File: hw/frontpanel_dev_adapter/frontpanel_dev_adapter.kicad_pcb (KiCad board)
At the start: 4 copper layers, 100 x 100 mm, 130 parts, among them J201 KLD-0202-A, J202 Conn_WR-FAST_01x04, J203 Molex_MicroFit_30-43045-0421, J301 FFC_conn_14p, J302 FFC_conn_14p, J303 JST_S2B-PH-SM4-TB, J501 Conn_01x20, J502 Conn_01x20, J503 SWD, J504 STX-3501-3N_(TTL-232R-xV-AJ), J601 Conn_02x32_Odd_Even, J602 Conn_02x32_Odd_Even, J603 Conn_02x32_Odd_Even, J604 Conn_02x32_Odd_Even, M401 Fan_4pin, Q201 Si4497DY, Q301 DMG1012T, Q401 DMG1012T, Q501 AO3401A, SW501 SKHUxxE010, U201 TPS54332DDA, U202 TLV1117LV30DCY, U203 TLV1117LV30DCY, U301 TLV9051SIDBV, U401 74LVC2G17gw, U501 STM32F103CBTx, U502 W25Q64FV, U503 CAT24C256, U504 DS3231MZ, Y501 8.0M

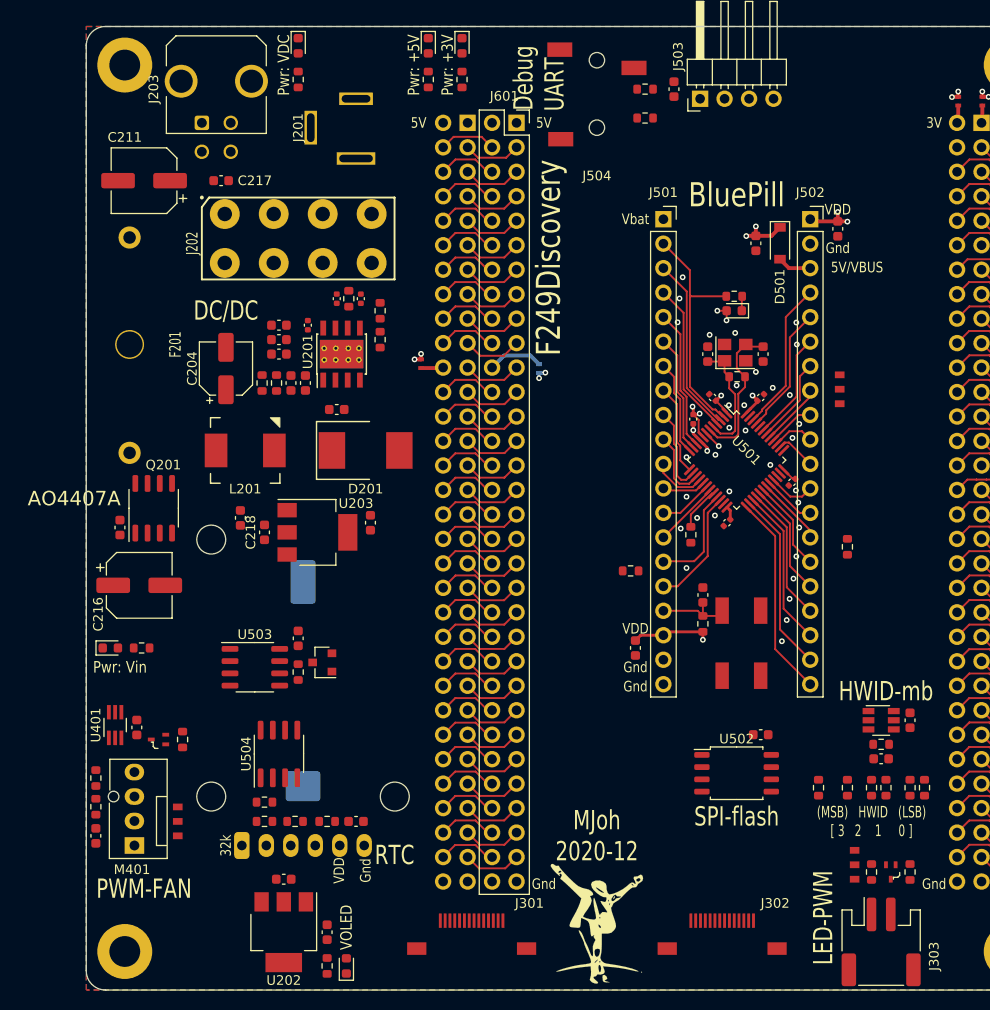
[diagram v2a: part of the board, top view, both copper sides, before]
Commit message: Frontpanel dev adapter: Optimize some LCSC components for JLC assembly; add some datasheets. Optimize F103 16MHz xtal routing
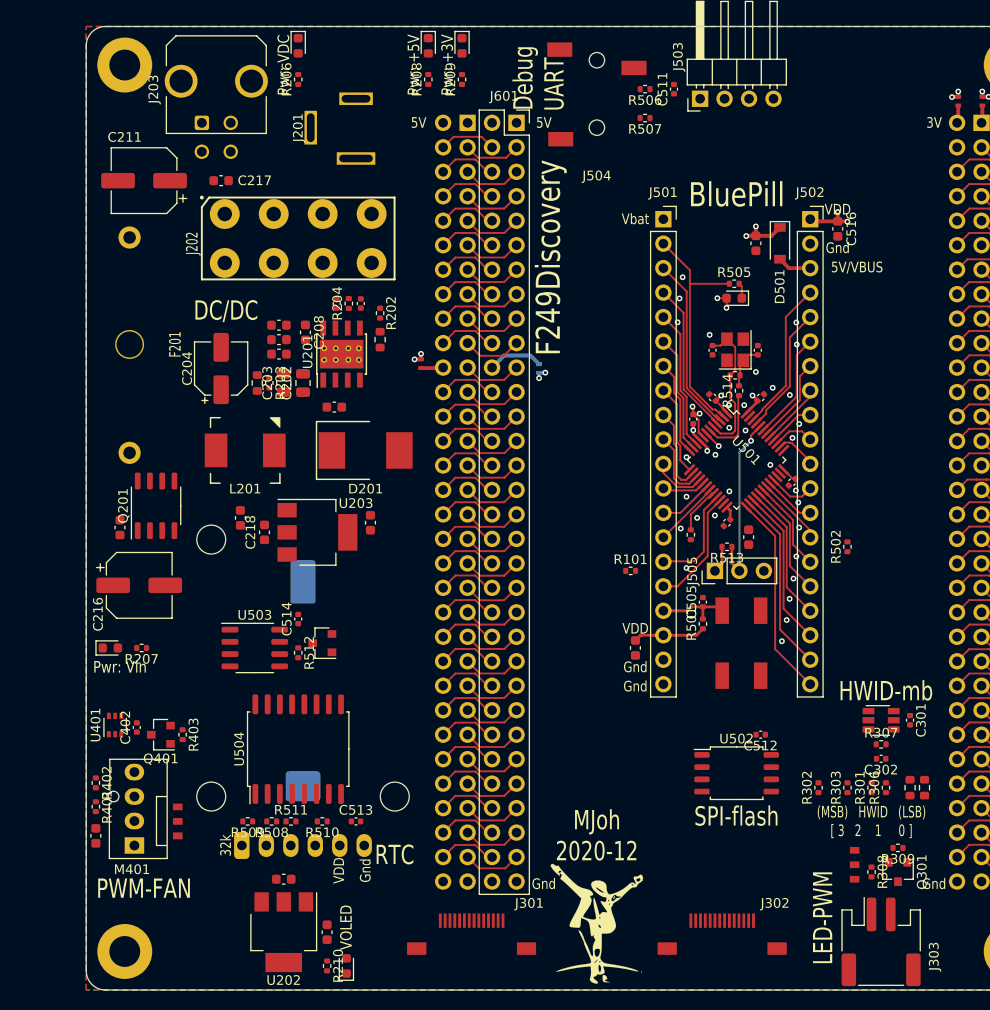
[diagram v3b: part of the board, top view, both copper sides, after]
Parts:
- removed JP501: dogbone_3_ud, customlib_mj_fp:db3_ud_0603
- added C516: 10u, Capacitor_SMD:C_0603_1608Metric, F.Cu at (128.0, 71.0)
- added J505: Conn_01x03, Connector_PinHeader_2.54mm:PinHeader_1x03_P2.54mm_Vertical, F.Cu at (115.2, 106.5)
- added R513: 0R, Resistor_SMD:R_0402_1005Metric, F.Cu at (116.5, 104.0)
- added R514: 47R, Resistor_SMD:R_0402_1005Metric, F.Cu at (117.8, 87.8)
- C202, C203: value 10u -> 10u/16V; footprint Capacitor_SMD:C_0603_1608Metric -> Capacitor_SMD:C_0805_2012Metric
- C205, C206, C207, C212, C218: value 10u -> 10u/10V
- C208: footprint Capacitor_SMD:C_0402_1005Metric -> Capacitor_SMD:C_0603_1608Metric
- C210: value 3n9 -> 3n3
- C301, C302, C402: footprint Capacitor_SMD:C_0603_1608Metric -> Capacitor_SMD:C_0402_1005Metric
- C501, C502, C503, C504, C515: value 0.1u -> 100n
- C505, C511, C512, C513, C514: value 0.1u -> 100n; footprint Capacitor_SMD:C_0603_1608Metric -> Capacitor_SMD:C_0402_1005Metric
- C506, C508: value 20p -> 12p; footprint Capacitor_SMD:C_0603_1608Metric -> Capacitor_SMD:C_0402_1005Metric
- D502: value Green -> White
- Q201: value Si4497DY -> AO4407A
- Q301, Q401: value DMG1012T -> AO3400A; footprint customlib_mj_fp:SOT-523_handsoldering -> Package_TO_SOT_SMD:SOT-23
- R101, R502: value 100 -> 100R; footprint Resistor_SMD:R_0603_1608Metric -> Resistor_SMD:R_0402_1005Metric
- R202, R203, R204, R301, R302, R303, R306, R307, R308, R309, R401, R402, R403, R501, R503, R504, R506, R507, R508, R509, R510, R511, R512: footprint Resistor_SMD:R_0603_1608Metric -> Resistor_SMD:R_0402_1005Metric
- R206, R207: value 4k7 -> 10k; footprint Resistor_SMD:R_0603_1608Metric -> Resistor_SMD:R_0402_1005Metric
- R208: value 1k -> 2k2; footprint Resistor_SMD:R_0603_1608Metric -> Resistor_SMD:R_0402_1005Metric
- R209, R210: value 100R -> 1k; footprint Resistor_SMD:R_0603_1608Metric -> Resistor_SMD:R_0402_1005Metric
- R505: value 1k -> 100R; footprint Resistor_SMD:R_0603_1608Metric -> Resistor_SMD:R_0402_1005Metric
- U401: footprint Package_TO_SOT_SMD:SOT-363_SC-70-6_Handsoldering -> Package_TO_SOT_SMD:SOT-363_SC-70-6
- U502: value W25Q64FV -> W25Q128JVSIQ
- U503: value CAT24C256 -> AT24C256C-SSHL
- U504: value DS3231MZ -> DS3231M; footprint Package_SO:SOIC-8_3.9x4.9mm_P1.27mm -> Package_SO:SOIC-16W_7.5x10.3mm_P1.27mm
- Y501: value 8.0M -> 16MHz
- moved C507 33.3 mm to (118.8, 103.0)
- moved R309 2.80 mm to (134.2, 135.2), turned to 180 degrees
- moved R509 2.65 mm to (66.8, 132.5)
- moved U504 2.06 mm to (72.0, 125.0)
- moved C514 2.00 mm to (72.0, 111.5)
- moved Q501 2.00 mm to (74.5, 114.0)
- moved R512 2.00 mm to (72.0, 115.0)
- moved U503 2.00 mm to (67.5, 114.5)
- moved D502 1.30 mm to (117.2, 78.2)
- moved R505 1.30 mm to (117.2, 76.7)
- moved C208 0.79 mm to (72.8, 81.8)
- moved C203 0.75 mm to (70.5, 87.0)
- moved C505 0.75 mm to (114.0, 109.8)
- moved Q301 0.75 mm to (134.2, 137.8), turned to 270 degrees
- moved R203 0.75 mm to (69.0, 87.0)
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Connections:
- U501 pad 44: GND -> Net-(J505-Pad2)
- U501 pad 6: Net-(C508-Pad1) -> Net-(R514-Pad1)
- U504 pad 2: VDD -> +BATT
- U504 pad 6: +BATT -> GND
- U504 pad 7: I2C1_SDA -> GND
- U504 pad 8: I2C1_SCL -> GND
- Y501 pad 1: Net-(C506-Pad1) -> Net-(C508-Pad1)
- Y501 pad 3: Net-(C508-Pad1) -> Net-(C506-Pad1)
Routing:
- net Net-(J505-Pad2): track 0.00 -> 18.7 mm, vias 0 -> 1
- net Net-(C508-Pad1): track 15.6 -> 4.56 mm
- net Net-(R514-Pad1): track 0.00 -> 7.44 mm
- net GND: track 4.29 -> 7.10 mm, vias 36 -> 34
- net Net-(C506-Pad1): track 12.2 -> 14.7 mm
- net VDD: track 34.5 -> 33.8 mm, vias 21 -> 20
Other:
- board text removed: "AO4407A"

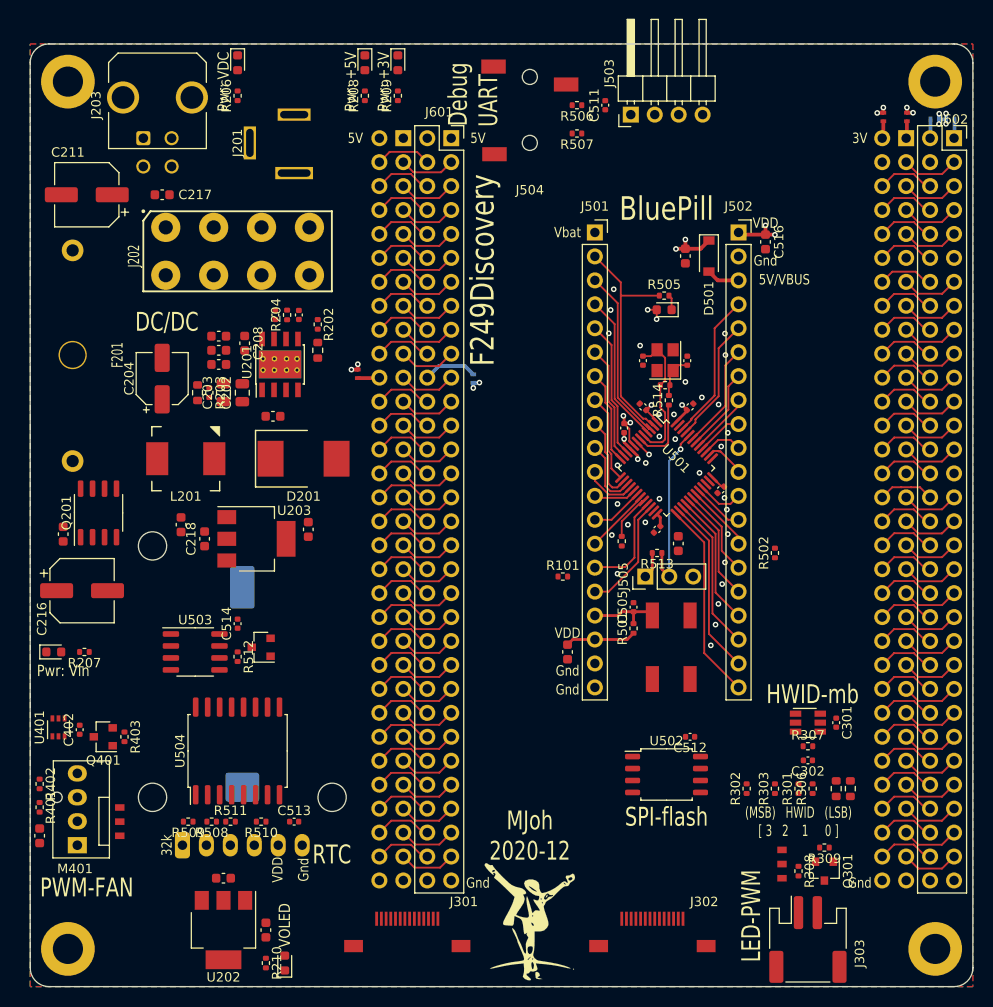
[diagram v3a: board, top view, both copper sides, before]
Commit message: FP adapter/dev board: *routing DONE* ; minor pinout tweaks (optimize routing); fix some missing 3d models
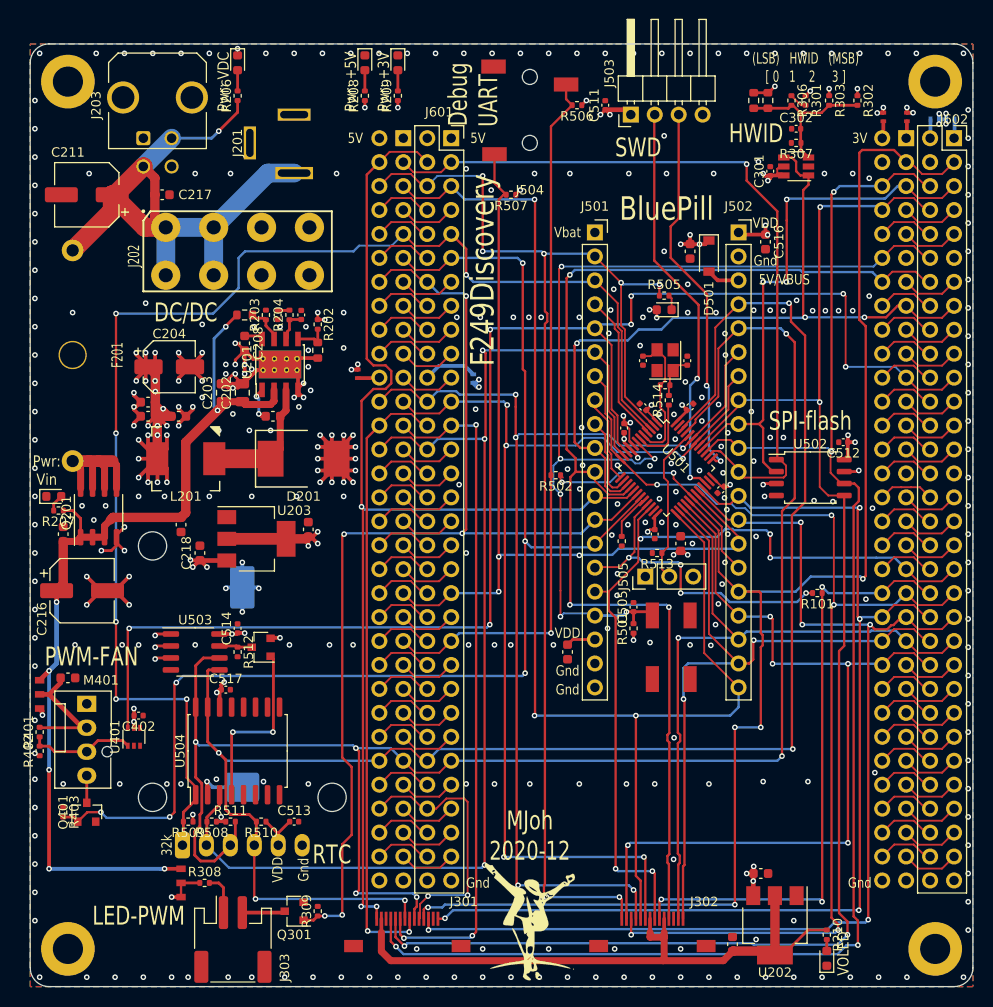
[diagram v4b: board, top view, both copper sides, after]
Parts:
- added C517: 100n, Capacitor_SMD:C_0402_1005Metric, F.Cu at (70.8, 118.5)
- moved R302 73.9 mm to (137.8, 56.0), turned to 270 degrees
- moved R305 73.7 mm to (126.8, 56.0), turned to 270 degrees
- moved R304 73.4 mm to (128.2, 56.0), turned to 270 degrees
- moved R303 73.2 mm to (134.8, 56.0), turned to 270 degrees
- moved R306 73.0 mm to (130.8, 56.0), turned to 270 degrees
- moved R301 73.0 mm to (132.2, 56.0), turned to 270 degrees
- moved C302 67.0 mm to (131.2, 59.0), turned to 0 degrees
- moved R307 64.0 mm to (131.2, 60.5), turned to 180 degrees
- moved JP301 63.8 mm to (66.0, 139.0), turned to 90 degrees
- moved R308 63.0 mm to (68.5, 139.0), turned to 0 degrees
- moved J303 61.0 mm to (71.5, 145.0)
- moved R210 59.6 mm to (134.5, 144.5)
- moved U301 59.0 mm to (131.2, 63.0), turned to 180 degrees
- moved C301 58.9 mm to (128.5, 63.5), turned to 90 degrees
- moved U202 58.5 mm to (129.0, 143.5)
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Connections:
- C401 pad 2: VMAIN -> Net-(C401-Pad2)
- J501 pad 10: HWID_FP -> HWID_MB
- J501 pad 11: HWID_MB -> HWID_FP
- J501 pad 8: ~FP_BTN_1An~ -> /MCU / Bluepill/PA3
- J501 pad 9: ~FP_BTN_1Bn~ -> /MCU / Bluepill/PA4
- J502 pad 12: /MCU / Bluepill/PA12 -> ~FP_BTN_1An~
- J502 pad 13: /MCU / Bluepill/PA11 -> ~FP_BTN_1Bn~
- J601 pad 58: /F429Discovery connection/PG8 -> ~FP_ENC2_SWn~
- J602 pad 54: ~FP_ENC2_SWn~ -> /F429Discovery connection/PD8
- J603 pad 58: /F429Discovery connection/PG8 -> ~FP_ENC2_SWn~
- J604 pad 54: ~FP_ENC2_SWn~ -> /F429Discovery connection/PD8
- JP401 pad 2: VMAIN -> Net-(C401-Pad2)
- M401 pad 2: VMAIN -> Net-(C401-Pad2)
- R401 pad 2: VMAIN -> Net-(C401-Pad2)
- SW501 pad 1: ~RSTn~ -> Net-(SW501-Pad1)
- U501 pad 13: ~FP_BTN_1An~ -> /MCU / Bluepill/PA3
- U501 pad 14: ~FP_BTN_1Bn~ -> /MCU / Bluepill/PA4
- U501 pad 15: HWID_FP -> HWID_MB
- U501 pad 16: HWID_MB -> HWID_FP
- U501 pad 32: /MCU / Bluepill/PA11 -> ~FP_BTN_1Bn~
- U501 pad 33: /MCU / Bluepill/PA12 -> ~FP_BTN_1An~
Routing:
- net I2C1_SCL: track 19.4 -> 184.3 mm, vias 0 -> 6
- net I2C1_SDA: track 21.8 -> 179.3 mm, vias 0 -> 5
- net DISP_FLASH_SCK: track 10.5 -> 161.3 mm, vias 0 -> 4
- net DISP_FLASH_MOSI: track 12.7 -> 159.0 mm, vias 0 -> 4
- net ~DISP_CSn~: track 17.9 -> 155.7 mm, vias 0 -> 5
- net FAN1_RPM: track 20.7 -> 156.6 mm, vias 0 -> 7
- net FAN1_PWM: track 13.0 -> 136.4 mm, vias 0 -> 6
- net 32k: track 24.4 -> 144.1 mm, vias 0 -> 6
- net HWID_FP: track 13.4 -> 127.3 mm, vias 0 -> 3
- net DISP_D~Cn~: track 10.5 -> 122.5 mm, vias 0 -> 3
- net ~SYS_RSTn~: track 27.3 -> 137.3 mm, vias 0 -> 3
- net ~RTC_INTn~_SQW: track 18.3 -> 128.2 mm, vias 0 -> 3
- net AUX_BOOT0: track 31.0 -> 137.3 mm, vias 0 -> 7
- net ~FP_BTN_1Bn~: track 15.1 -> 120.7 mm, vias 0 -> 5
- net PWRBTN_LED_PWM: track 11.7 -> 114.7 mm, vias 0 -> 5
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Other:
- board text added: "(LSB) HWID (MSB) [ 0 1 2 3 ]"
- board text added: "HWID"
- board text added: "SWD"
- board text removed: "(MSB) HWID (LSB) [ 3 2 1 0 ]"
- board text removed: "HWID-mb"

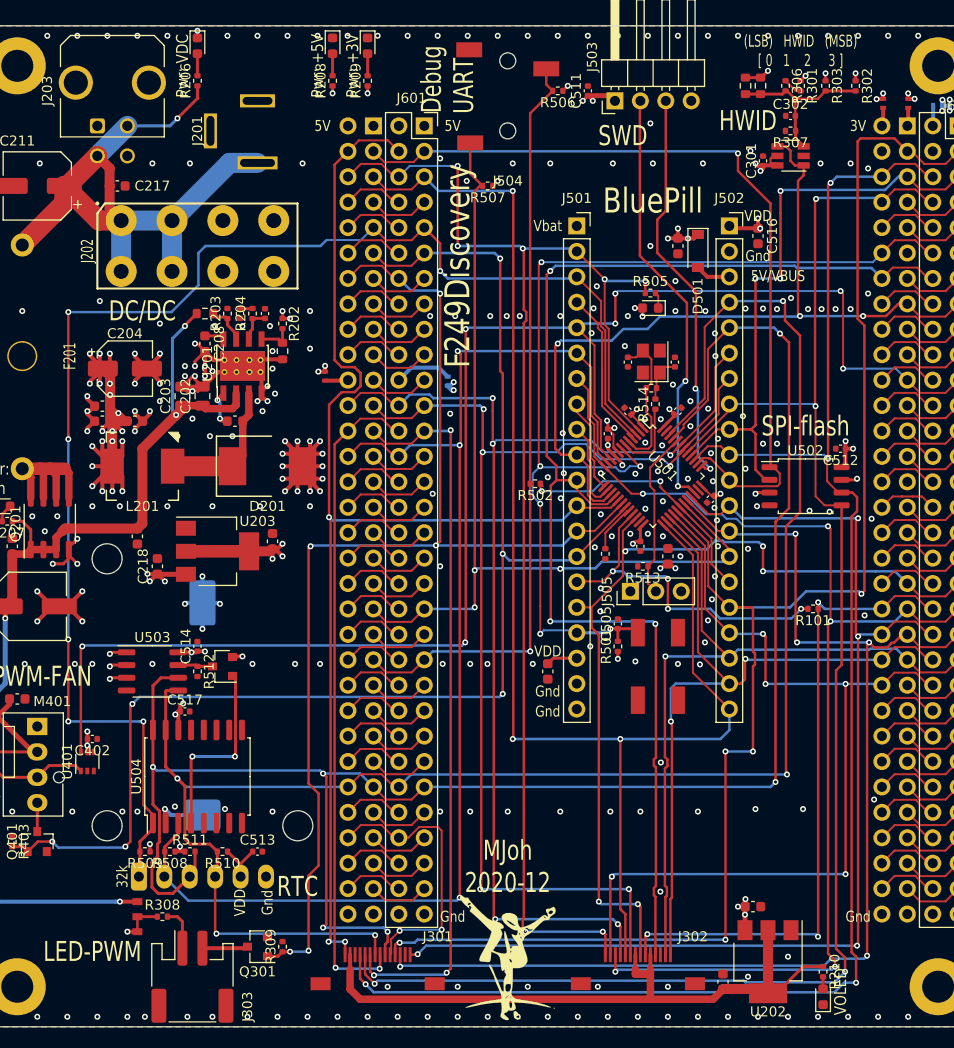
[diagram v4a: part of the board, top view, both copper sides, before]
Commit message: FP adapter: Add JLCPCB serial string; tooling holes; route Vin to buck on bottom instead of directly under inductor
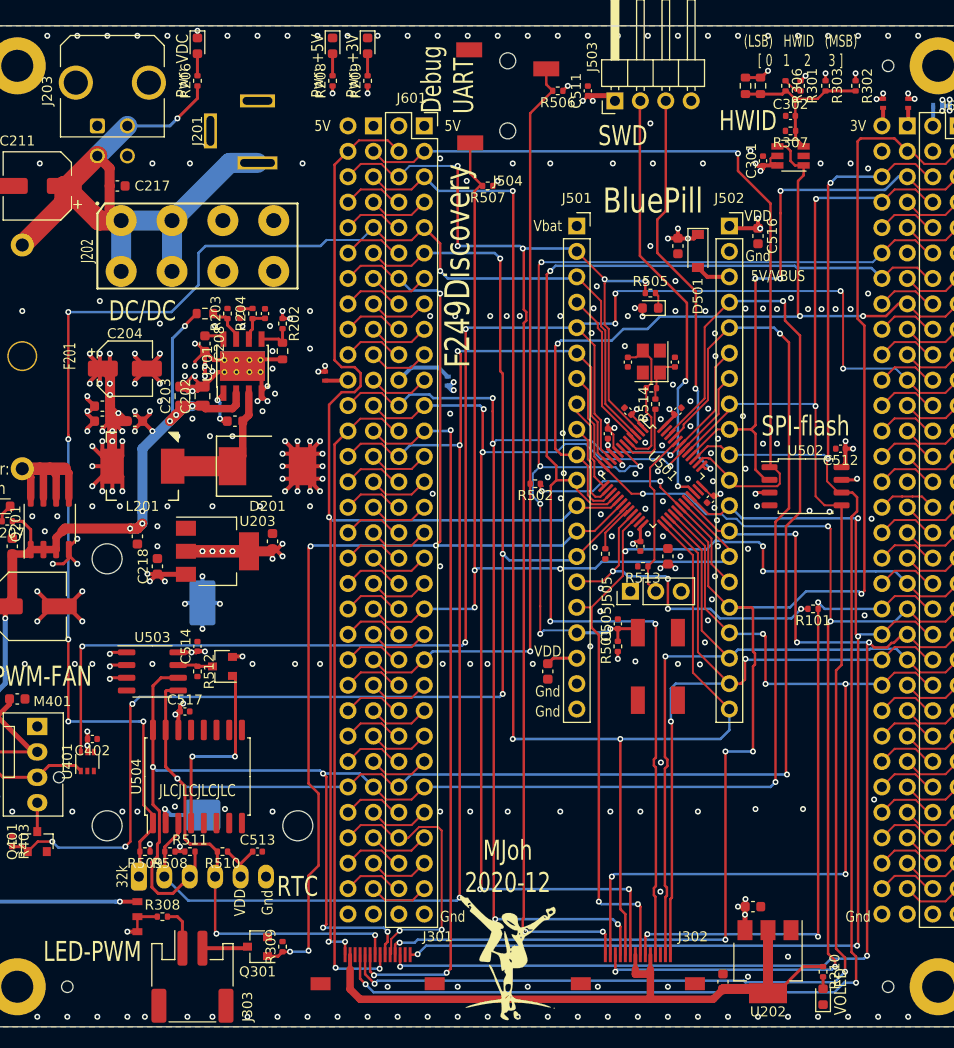
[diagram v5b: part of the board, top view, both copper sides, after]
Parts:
- added M101: JLC_tooling_hole, customlib_mj_fp:JLC_tooling-hole, F.Cu at (59.0, 146.0)
- added M102: JLC_tooling_hole, customlib_mj_fp:JLC_tooling-hole, F.Cu at (141.0, 146.0)
- added M103: JLC_tooling_hole, customlib_mj_fp:JLC_tooling-hole, F.Cu at (141.0, 54.0)
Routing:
- net VIN: track 101.1 -> 105.4 mm, vias 7 -> 12
- net GND: track 109.5 -> 110.9 mm, vias 331 -> 334
- net VDD: vias 55 -> 59
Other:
- board text added: "JLCJLCJLCJLC"
